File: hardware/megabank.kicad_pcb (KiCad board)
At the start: 4 copper layers, 130 x 56 mm, 89 parts, among them J1 USB-C, P1 TS2068_Edge, Q1 AO3401A, Q2 AO3400A, SW3 RUN, SW4 BOOTSEL, SW5 WP, U1 74LVC245APW, U10 CY62167EV30LL-45ZXIT, U11 CY62167EV30LL-45ZXIT, U12 SN74LVC1G32DBVR, U2 74LVC245APW, U20 RP2350B, U21 GD25Q128ESIGR, U3 74LVC245APW, U30 TLV1117LV33, U31 TPS3839G33, U32 LM66200, U4 74LVC245APW, U5 74LVC1G06, Y1 12MHz

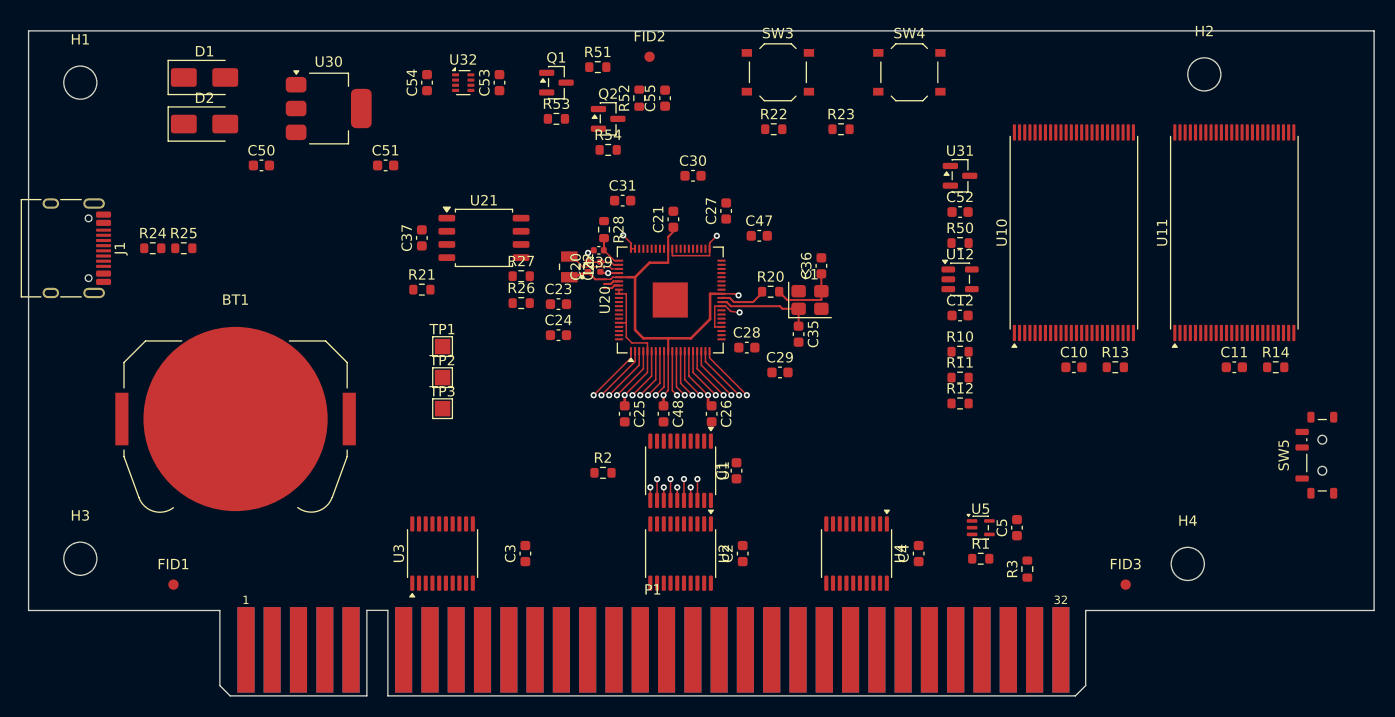
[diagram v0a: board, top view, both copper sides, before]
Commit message: Board: routed, DRC clean; render in the README
Routed by v3's flow.py with Freerouting 2.4.1, no hand edits: 1768 track
segments, 326 vias (all 0.6/0.3 mm), DRC clean at every severity.

One v3 pre-route changed: v3 drops supply pin 29 into the lanes of pads
27/28, spare there, but here they are nDOE and BE_REQ, and every attempt
left both sealed in. The 24/29 link now runs under the package to pin 15.
finish.py no longer crashes when its lift-and-retry backup is missing.

The top and bottom renders are in docs/images; the README shows the top.

Co-Authored-By: Claude Opus 5.5 <noreply@anthropic.com>
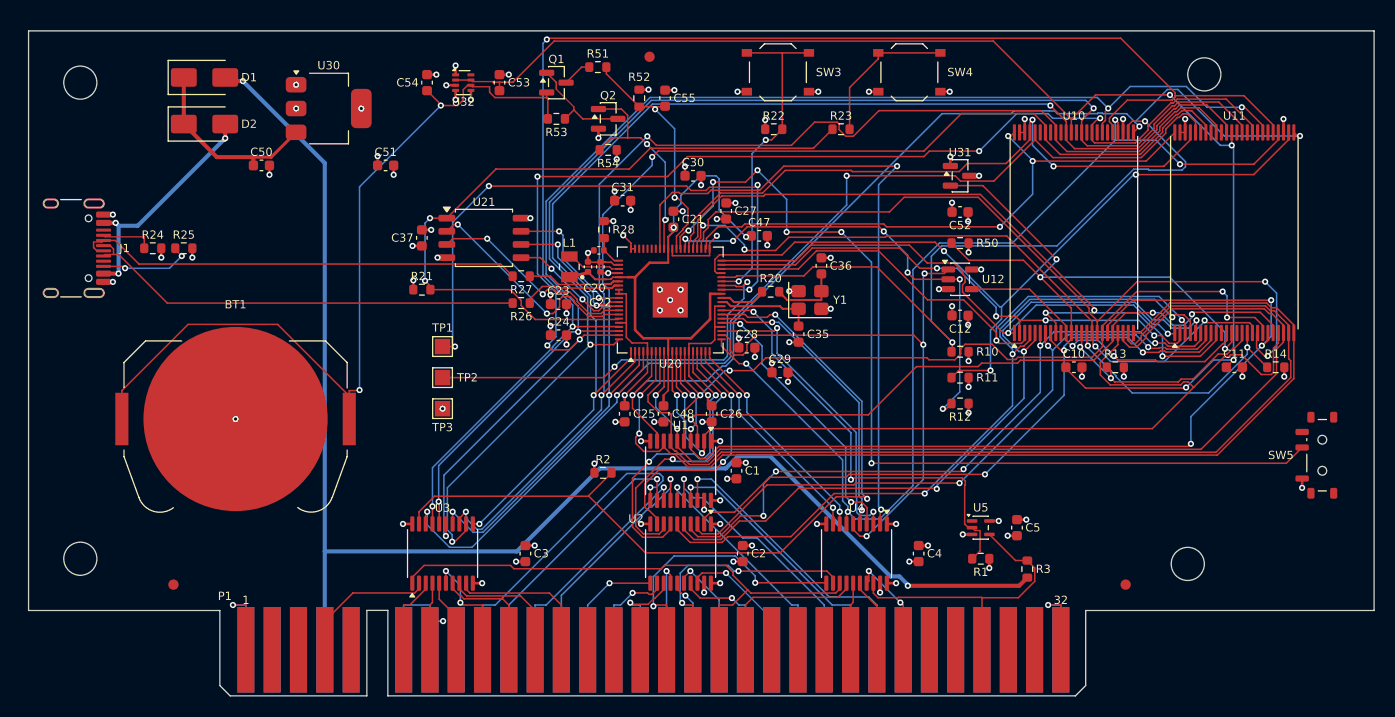
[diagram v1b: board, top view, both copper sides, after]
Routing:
- net SD0: track 0.00 -> 141.7 mm, vias 0 -> 3
- net +5V_EDGE: track 0.00 -> 137.3 mm, vias 0 -> 2
- net SD2: track 0.00 -> 129.7 mm, vias 0 -> 6
- net VSRAM: track 0.00 -> 126.2 mm, vias 0 -> 4
- net SD3: track 0.00 -> 125.6 mm, vias 0 -> 3
- net SD1: track 0.00 -> 121.9 mm, vias 0 -> 4
- net SD4: track 5.74 -> 119.2 mm, vias 1 -> 3
- net SD5: track 5.60 -> 118.6 mm, vias 1 -> 3
- net SD6: track 5.45 -> 114.9 mm, vias 1 -> 3
- net SD7: track 5.31 -> 108.5 mm, vias 1 -> 3
- net GND: track 4.60 -> 105.5 mm, vias 1 -> 82
- net nRD_L: track 0.00 -> 98.6 mm, vias 0 -> 4
- net BA1: track 4.87 -> 101.5 mm, vias 1 -> 2
- net BA2: track 4.73 -> 99.3 mm, vias 1 -> 0
- net BA3: track 4.58 -> 96.2 mm, vias 1 -> 2
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
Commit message: Board: /INT and /NMI for the controller (open question 16)
- U7 SN74LVC2G34 brings /INT (A14) and /NMI (A15) to GPIO43/44.
- U6, a second 74LVC1G06, pulls /NMI from GPIO45 (NMI_REQ), open-drain
  like /BE; R4 holds NMI_REQ low until the firmware runs.
- Placed over fingers A14/A15 between C3 and U2. Re-routed by flow.py
  (closed on attempt 2): DRC clean, nothing unconnected; ERC has the one
  expected warning. BOMs and renders regenerated.
- Spec: pin table (46 of 48, now counting the /BE read-back), parts,
  open question 16 marked added.

Co-Authored-By: Claude Opus 5.5 <noreply@anthropic.com>
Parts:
- added C6: 100n, C_0603_1608Metric, F.Cu at (56.5, 51.5)
- added C7: 100n, C_0603_1608Metric, F.Cu at (51.5, 51.5)
- added R4: 10k, R_0603_1608Metric, F.Cu at (56.5, 45.2)
- added U6: 74LVC1G06, SOT-353_SC-70-5, F.Cu at (56.5, 48.0)
- added U7: 74LVC2G34, SOT-363_SC-70-6, F.Cu at (51.5, 48.0)
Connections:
- P1 pad A14: unconnected-(P1-~{INT}-PadA14) -> /2068 Interface/nINT
- P1 pad A15: unconnected-(P1-~{NMI}-PadA15) -> /2068 Interface/nNMI
- U20 pad 54: unconnected-(U20-GPIO43/ADC3-Pad54) -> nINT_L
- U20 pad 55: unconnected-(U20-GPIO44/ADC4-Pad55) -> nNMI_L
- U20 pad 56: unconnected-(U20-GPIO45/ADC5-Pad56) -> NMI_REQ
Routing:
- net nNMI_L: track 0.00 -> 69.4 mm, vias 0 -> 2
- net nINT_L: track 0.00 -> 55.0 mm, vias 0 -> 6
- net NMI_REQ: track 0.00 -> 39.1 mm, vias 0 -> 4
- net nDOE: track 79.7 -> 57.8 mm
- net /2068 Interface/nNMI: track 0.00 -> 21.8 mm, vias 0 -> 2
- net SD3: track 125.6 -> 146.8 mm, vias 3 -> 6
- net BA7: track 74.6 -> 95.1 mm, vias 4 -> 6
- net BA13: track 29.4 -> 48.5 mm
- net BA5: track 73.4 -> 91.1 mm, vias 4 -> 3
- net /2068 Interface/nINT: track 0.00 -> 15.2 mm, vias 0 -> 2
- net VSRAM: track 126.2 -> 141.0 mm, vias 4 -> 2
- net /SRAM/nSWE: track 30.4 -> 43.8 mm, vias 2 -> 3
- net BA8: track 63.8 -> 76.9 mm
- net nBE_L: track 64.2 -> 51.3 mm, vias 2 -> 4
- net /RP2350B Controller/SWDIO: track 39.1 -> 50.7 mm
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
